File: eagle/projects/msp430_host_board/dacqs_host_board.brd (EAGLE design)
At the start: 127 x 102 mm, 165 parts, among them J1 MOL-SL-4-RA, J10 MOL-SL-3-V, J13 JST-PH-2TH-RA, J14 USB_MICROB_RECPT, J16 MOL-SL-2-RA, J17 CLM-112-02-L-D-IMU-MOUNT_IMU, J18 MOLSL-7-RA, J2 MOL-SL-4-RA, J3 MOL-SL-4-RA, J4 MOL-SL-4-RA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

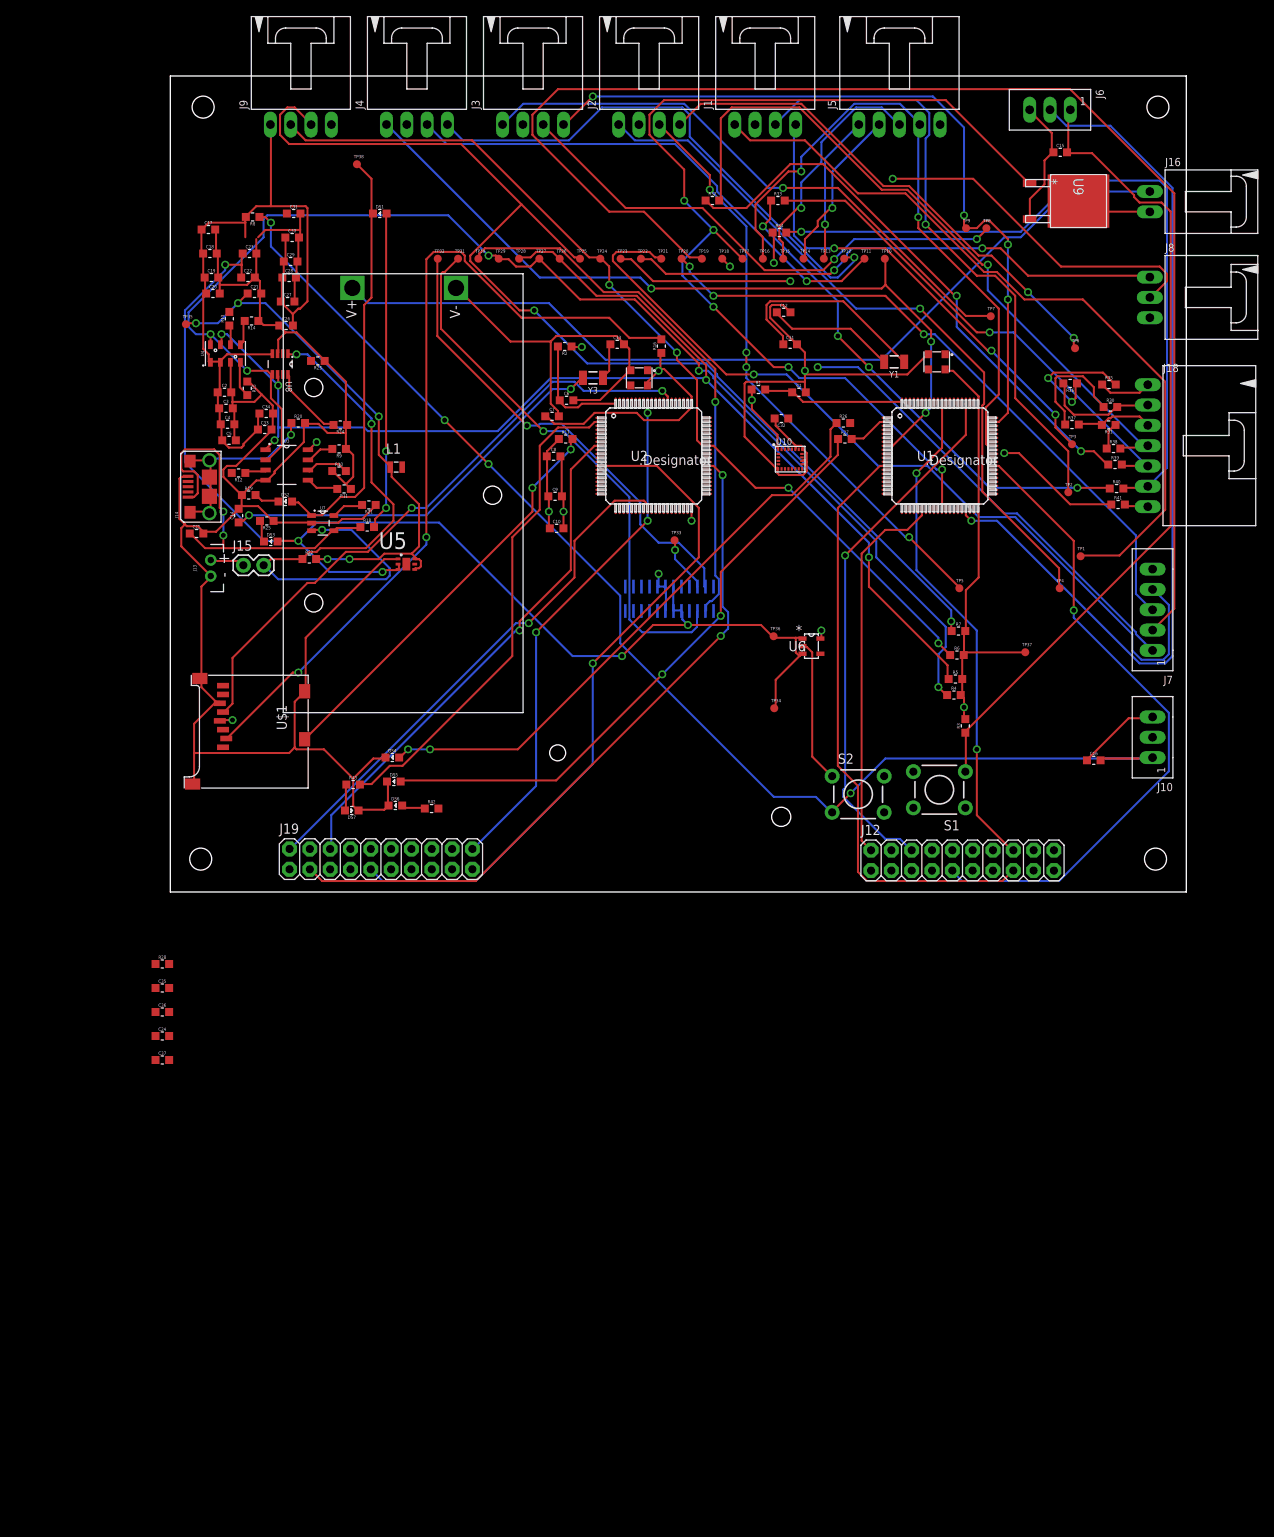
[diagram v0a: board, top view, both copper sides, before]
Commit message: Changed motor battery Vsense
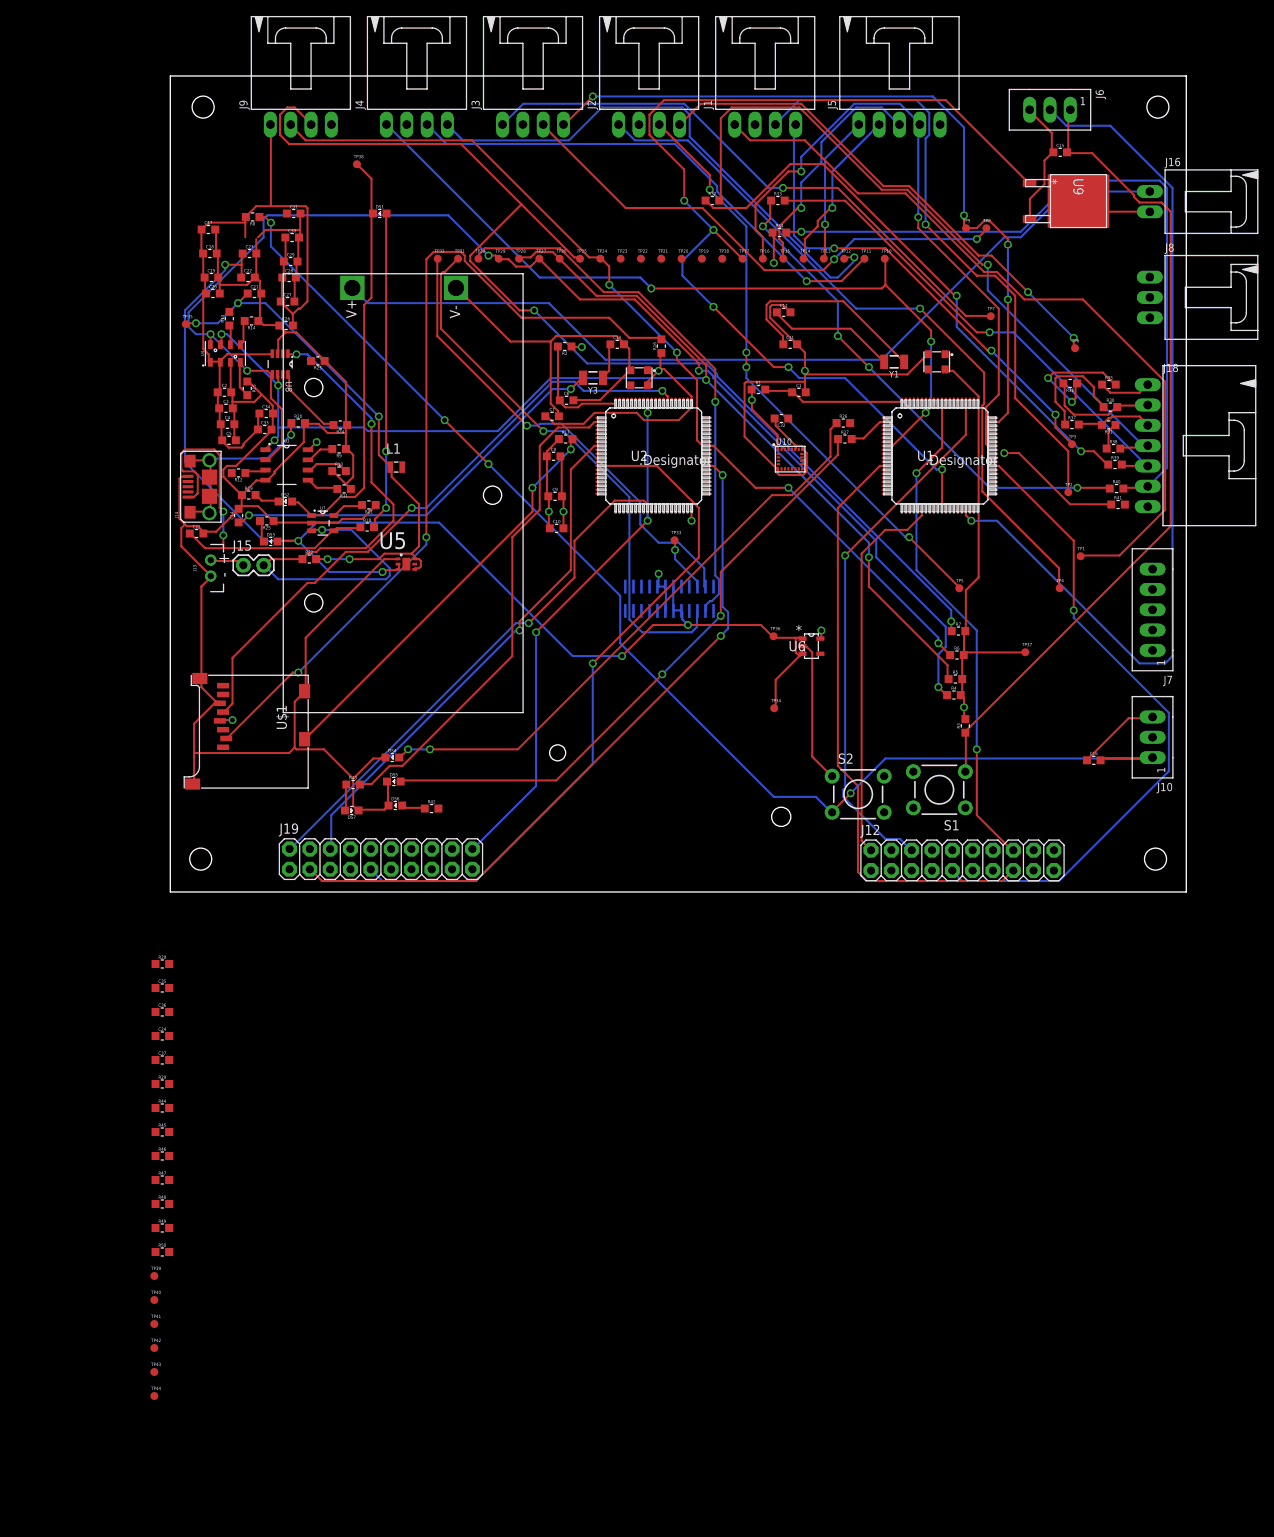
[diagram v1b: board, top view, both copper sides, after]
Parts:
- added R29, R44, R45, R46, R47, R48: 0, daqcs_host:R0603
- added R49, R50: 47k, daqcs_host:R0603
- added TP39, TP40, TP41, TP42, TP43, TP44: (no value), daqcs_host:TP10R
- R30: value 10k -> 60.4k
- R31: value 10k -> 69.8k
- R32, R33, R35: value 10k -> 49.9k
- R34: value 10k -> 12k
- R36: value 27k -> 7.15k
- R37: value 27k -> 10k
- R38, R39: value 27k -> 15k
- R40, R41: value 27k -> 30k
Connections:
- removed net VBAT_CELL_7: J18.7, R41.2
- new net ACT_CURRENT_IN_0: J8.2, R44.1
- new net ACT_SPEED_IN_0: J8.1, R29.1
- new net COMMS_MISO_0: J7.3, R47.1
- new net COMMS_MOSI_0: J7.4, R48.1
- new net COMMS_SCLK_0: J7.2, R46.1
- new net COMMS_SS_0: J7.1, R45.1
- new net RST_S1: R49.1, S1.3
- new net RST_S2: R50.1, S2.3
- net +3V3: now also J12.2
- net ACT_CURRENT_IN: now also R44.2; no longer J8.2
- net ACT_SPEED_IN: now also R29.2; no longer J8.1
- net COMMS_MISO: now also R47.2, TP20.TP
- net COMMS_MOSI: now also R48.2, TP21.TP
- net COMMS_SCLK: now also R46.2, TP19.TP
- net COMMS_SS: now also R45.2, TP18.TP
- net CURRENT_PWM_OUT: no longer J7.2, TP19.TP
- net DIR_MOTOR_OUT: no longer J7.4, TP21.TP
- net EN_MOTOR_OUT: no longer J7.3, TP20.TP
- net GND: now also J12.20, J18.7, TP39.TP, TP41.TP, TP42.TP, TP43.TP, TP44.TP
- net P2.3: no longer J12.4
- net P2.4: no longer J12.6
- net P4.1: now also J12.6; no longer J12.8
- net P6.2: now also J12.8; no longer J12.10
- net P6.3: now also J12.10; no longer J12.12
- net P6.4: now also J12.12; no longer J12.14
- net P6.5: now also J12.14; no longer J12.16
- net P6.6: now also J12.16; no longer J12.18
- net P6.7: now also J12.18; no longer J12.20
- net P7.3: now also J12.4; no longer J12.2
- net RST_SBWTDIO_HOST: now also R49.2; no longer S1.3
- net RST_SBWTDIO_MOTOR: now also R50.2; no longer S2.3
- net SPEED_PWM_OUT: no longer J7.1, TP18.TP
- net VBAT_CELL_2: no longer R36.2
- net VBAT_CELL_3: no longer R37.2
- net VBAT_CELL_4: no longer R38.2
- net VBAT_CELL_5: no longer R39.2
- net VBAT_CELL_6: no longer R40.2
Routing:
- net CURRENT_PWM_OUT: track 172.8 -> 0.00 mm
- net DIR_MOTOR_OUT: track 107.9 -> 0.00 mm, vias 1 -> 0
- net ACT_CURRENT_IN: track 83.6 -> 0.00 mm, vias 2 -> 0
- net EN_MOTOR_OUT: track 81.8 -> 0.00 mm, vias 3 -> 0
- net SPEED_PWM_OUT: track 75.2 -> 0.00 mm, vias 2 -> 0
- net ACT_SPEED_IN: track 67.5 -> 0.00 mm, vias 2 -> 0
- net VBAT_CELL_7: track 3.06 -> 0.00 mm

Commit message: Added optocoupler isolation for cutdown mechanism
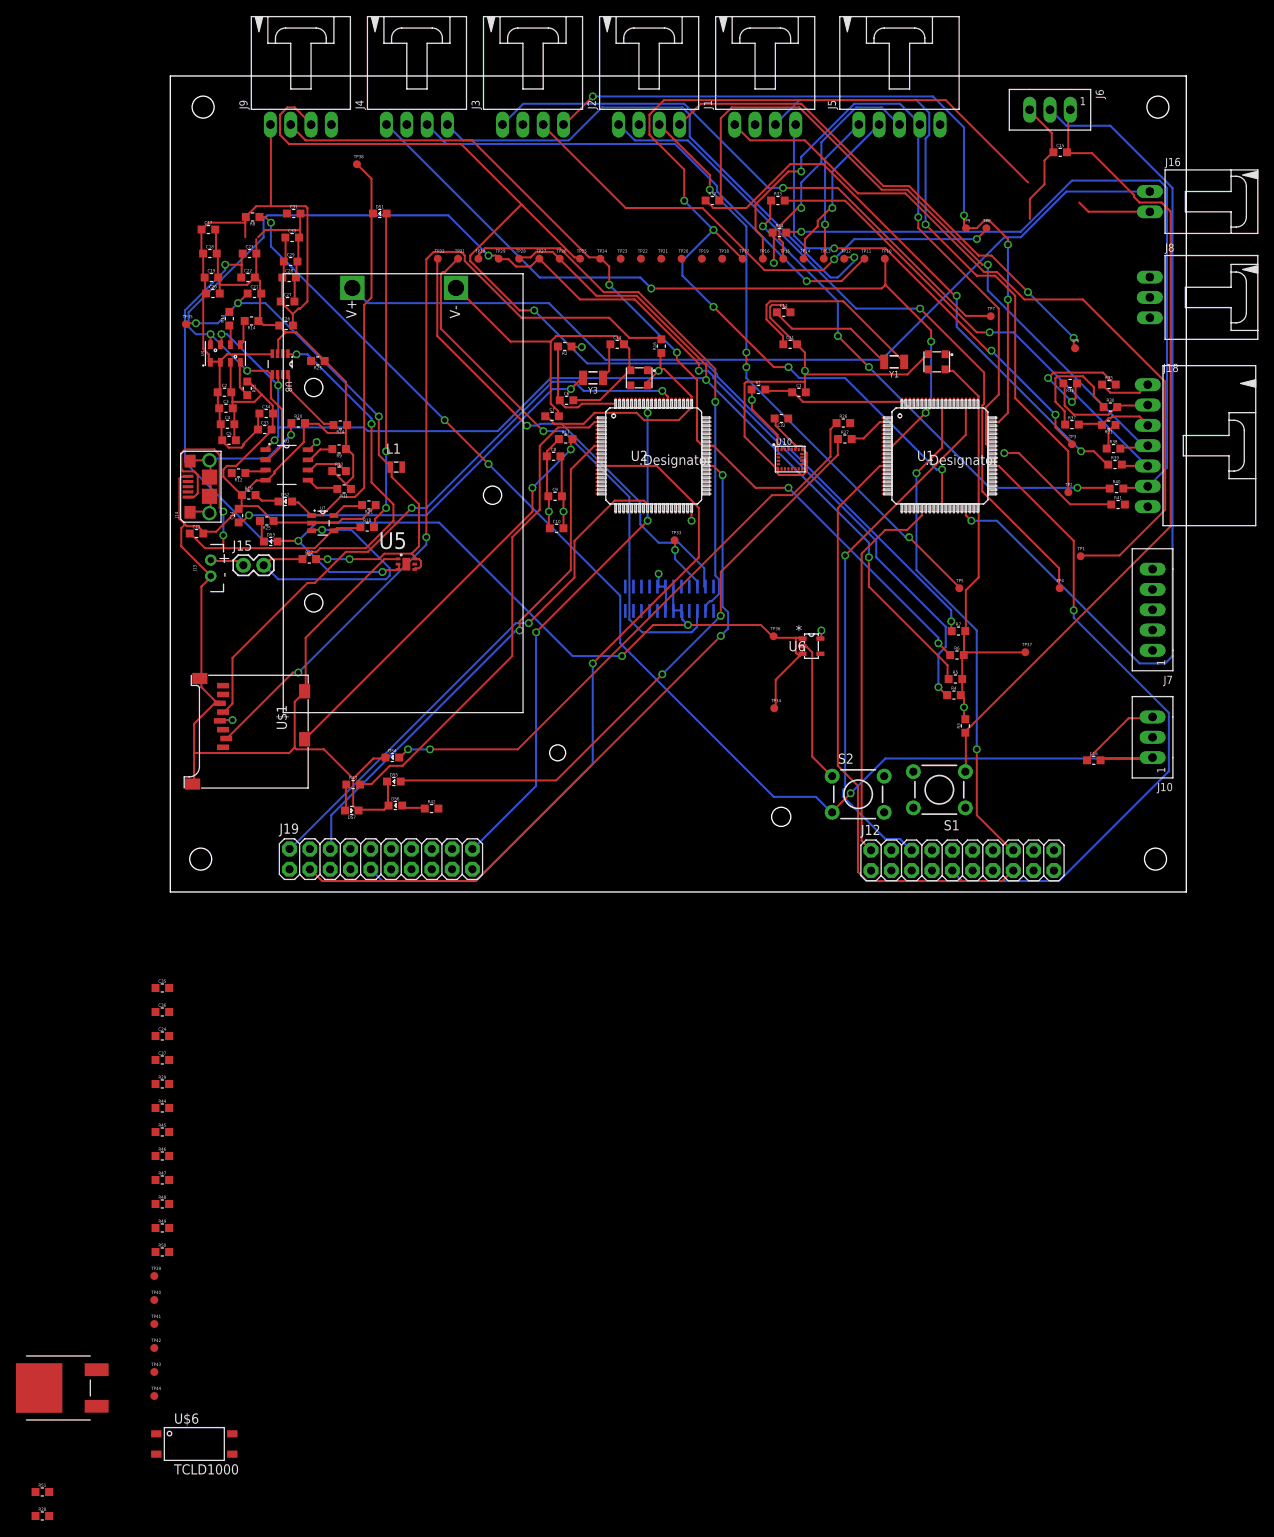
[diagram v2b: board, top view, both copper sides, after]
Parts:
- removed U9: STD12NF06LT4, daqcs_host:DPAK
- added R51: 47k, daqcs_host:R0603
- added U$6: TCLD1000, daqcs_host:TCLD1000
- added U$7: NTD2955T4G, daqcs_host:NTD2955T4G
- R28: value 10k -> 49.9k
- moved R28 70.6 mm to (-16.0, -78.0)
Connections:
- new net N$37: BAT1.V-, U$6.P$4, U$7.P$3
- new net N$59: R28.2, U$6.P$2
- net CUTDOWN_EN: now also R51.1, U$6.P$1, U$6.P$3, U$7.P$1; no longer R28.2, U9.1
- net GND: no longer BAT1.V-, U9.2
- net N$6: now also R51.2, U$7.P$2; no longer U9.3

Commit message: Pinned the IMU2 interrupt signals to the GPIO headers
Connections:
- removed net N$22: U10.9
- removed net N$23: U10.10
- removed net N$7: U10.11
- removed net N$8: U10.12
- removed net N$9: U10.13
- new net IMU2_DEN: J12.11, U10.13
- new net IMU2_DRDY: J12.13, U10.9
- new net IMU2_INT1: J12.7, U10.11
- new net IMU2_INT2: J12.9, U10.12
- new net IMU2_INT_M: J12.15, U10.10
- new net N$60: U1.27
- net P3.4: no longer J12.7
- net P3.5: no longer J12.9
- net P4.1: no longer J12.6
- net P5.6: no longer J12.11
- net P5.7: no longer J12.13
- net P7.0: now also J12.17; no longer J12.15
- net P7.1: now also J12.19; no longer J12.17
- net P7.2: now also J12.4; no longer J12.19
- net P7.3: now also J12.6; no longer J12.4
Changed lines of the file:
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@@
 <signal name="P7.0">
 <contactref element="U1" pad="13"/>
-<contactref element="J12" pad="15"/>
 <wire x1="88.6968" y1="53.2638" x2="89.3826" y2="53.2638" width="0.254" layer="1"/>
 <wire x1="83.439" y1="48.006" x2="88.6968" y2="53.2638" width="0.254" layer="1"/>
@@
 <wire x1="105.156" y1="2.5146" x2="104.013" y2="1.3716" width="0.254" layer="1"/>
 <wire x1="89.3826" y1="53.2638" x2="89.475" y2="53.27" width="0.254" layer="1"/>
-<wire x1="105.156" y1="2.5146" x2="105.37" y2="2.68" width="0.254" layer="1"/>
+<contactref element="J12" pad="17"/>
+<wire x1="105.156" y1="2.5146" x2="107.91" y2="2.68" width="0" layer="19" extent="1-1"/>
 </signal>
 <signal name="P7.1">
 <contactref element="U1" pad="14"/>
-<contactref element="J12" pad="17"/>
-<wire x1="107.91" y1="2.68" x2="89.475" y2="52.77" width="0" layer="19" extent="1-1"/>
+<contactref element="J12" pad="19"/>
+<wire x1="110.45" y1="2.68" x2="89.475" y2="52.77" width="0" layer="19" extent="1-1"/>
 </signal>
 <signal name="P7.2">
 <contactref element="U1" pad="25"/>
-<contactref element="J12" pad="19"/>
-<wire x1="110.45" y1="2.68" x2="93.45" y2="47.795" width="0" layer="19" extent="1-1"/>
+<contactref element="J12" pad="4"/>
+<wire x1="90.13" y1="5.22" x2="93.45" y2="47.795" width="0" layer="19" extent="1-1"/>
 </signal>
 <signal name="P7.3">
@@
 <wire x1="87.5538" y1="5.2578" x2="86.4108" y2="6.4008" width="0.254" layer="1"/>
 <wire x1="93.9546" y1="47.7774" x2="93.95" y2="47.795" width="0.254" layer="1"/>
-<contactref element="J12" pad="4"/>
-<wire x1="87.5538" y1="5.2578" x2="90.13" y2="5.22" width="0" layer="19" extent="1-1"/>
+<contactref element="J12" pad="6"/>
+<wire x1="87.5538" y1="5.2578" x2="92.67" y2="5.22" width="0" layer="19" extent="1-1"/>
 </signal>
 <signal name="P3.4">
 <contactref element="U1" pad="47"/>
-<contactref element="J12" pad="7"/>
-<wire x1="95.21" y1="2.68" x2="102.925" y2="52.77" width="0" layer="19" extent="1-1"/>
 </signal>
 <signal name="P3.5">
 <contactref element="U1" pad="48"/>
-<contactref element="J12" pad="9"/>
 <wire x1="103.5558" y1="53.2638" x2="103.0986" y2="53.2638" width="0.254" layer="1"/>
 <wire x1="112.9284" y1="43.8912" x2="103.5558" y2="53.2638" width="0.254" layer="1"/>
@@
 <wire x1="97.8408" y1="2.5146" x2="98.9838" y2="1.3716" width="0.254" layer="16"/>
 <wire x1="103.0986" y1="53.2638" x2="102.925" y2="53.27" width="0.254" layer="1"/>
-<wire x1="97.8408" y1="2.5146" x2="97.75" y2="2.68" width="0.254" layer="16"/>
 <via x="112.9284" y="35.2044" extent="1-16" drill="0.6096"/>
 </signal>
 <signal name="P5.6">
 <contactref element="U1" pad="67"/>
-<contactref element="J12" pad="11"/>
-<wire x1="100.29" y1="2.68" x2="97.95" y2="61.245" width="0" layer="19" extent="1-1"/>
 </signal>
 <signal name="P5.7">
 <contactref element="U1" pad="68"/>
-<contactref element="J12" pad="13"/>
-<wire x1="102.83" y1="2.68" x2="97.45" y2="61.245" width="0" layer="19" extent="1-1"/>
 </signal>
 <signal name="P2.3">
@@
 <signal name="P4.1">
 <contactref element="U1" pad="32"/>
-<contactref element="J12" pad="6"/>
-<wire x1="92.67" y1="5.22" x2="96.95" y2="47.795" width="0" layer="19" extent="1-1"/>
 </signal>
 <signal name="N$10">
@@
 <wire x1="14.57" y1="84.81" x2="76.405" y2="55.335" width="0" layer="19" extent="1-1"/>
 </signal>
-<signal name="N$7">
+<signal name="IMU2_INT1">
 <contactref element="U10" pad="11"/>
-</signal>
-<signal name="N$8">
+<contactref element="J12" pad="7"/>
+<wire x1="95.21" y1="2.68" x2="78.125" y2="52.885" width="0" layer="19" extent="1-1"/>
+</signal>
+<signal name="IMU2_INT2">
 <contactref element="U10" pad="12"/>
-</signal>
-<signal name="N$9">
+<contactref element="J12" pad="9"/>
+<wire x1="97.75" y1="2.68" x2="78.555" y2="52.885" width="0" layer="19" extent="1-1"/>
+</signal>
+<signal name="IMU2_DEN">
 <contactref element="U10" pad="13"/>
-</signal>
-<signal name="N$22">
+<contactref element="J12" pad="11"/>
+<wire x1="100.29" y1="2.68" x2="78.985" y2="52.885" width="0" layer="19" extent="1-1"/>
+</signal>
+<signal name="IMU2_DRDY">
 <contactref element="U10" pad="9"/>
-</signal>
-<signal name="N$23">
+<contactref element="J12" pad="13"/>
+<wire x1="102.83" y1="2.68" x2="77.265" y2="52.885" width="0" layer="19" extent="1-1"/>
+</signal>
+<signal name="IMU2_INT_M">
 <contactref element="U10" pad="10"/>
+<contactref element="J12" pad="15"/>
+<wire x1="105.37" y1="2.68" x2="77.695" y2="52.885" width="0" layer="19" extent="1-1"/>
 </signal>
 <signal name="N$47">
@@
 <wire x1="-1.75" y1="-70.27" x2="-15.15" y2="-78" width="0" layer="19" extent="1-1"/>
 </signal>
+<signal name="N$60">
+<contactref element="U1" pad="27"/>
+</signal>
 </signals>

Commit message: Small change
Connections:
- net N$37 renamed 9V_GND
- net N$59 renamed OPTO_OUT
- net N$6 renamed CUTDOWN_DRAIN
- new net CUTDOWN_GATE: R51.1, U$6.P$3, U$7.P$1
- net CUTDOWN_EN: no longer R51.1, U$6.P$3, U$7.P$1
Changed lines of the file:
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@@
 <via x="77.2668" y="65.6082" extent="1-16" drill="0.6096"/>
 <via x="67.8942" y="73.152" extent="1-16" drill="0.6096"/>
-<contactref element="U$7" pad="P$1"/>
-<contactref element="R51" pad="1"/>
-<contactref element="U$6" pad="P$3"/>
 <contactref element="U$6" pad="P$1"/>
 <contactref element="TP17" pad="TP"/>
 <wire x1="71.3232" y1="79.3242" x2="71.53" y2="79.16" width="0" layer="19" extent="1-1"/>
-<wire x1="7.75" y1="-70.27" x2="96.45" y2="47.795" width="0" layer="19" extent="1-1"/>
-<wire x1="-1.75" y1="-67.73" x2="7.75" y2="-70.27" width="0" layer="19" extent="1-1"/>
-<wire x1="-9.21" y1="-64.285" x2="-1.75" y2="-67.73" width="0" layer="19" extent="1-1"/>
-<wire x1="-16.85" y1="-75" x2="-9.21" y2="-64.285" width="0" layer="19" extent="1-1"/>
+<wire x1="-1.75" y1="-67.73" x2="96.45" y2="47.795" width="0" layer="19" extent="1-1"/>
 </signal>
 <signal name="VBAT_MOD_CELL_1">
@@
 <wire x1="22.86" y1="75.438" x2="22.754" y2="75.506" width="0.254" layer="16"/>
 </signal>
-<signal name="N$6">
+<signal name="CUTDOWN_DRAIN">
 <contactref element="J16" pad="2"/>
 <wire x1="114.7572" y1="85.0392" x2="122.301" y2="85.0392" width="0.254" layer="1"/>
@@
 <wire x1="-1.85" y1="-45" x2="82.7288" y2="9.9594" width="0" layer="19" extent="1-1"/>
 </signal>
-<signal name="N$37">
+<signal name="9V_GND">
 <contactref element="U$7" pad="P$3"/>
 <contactref element="BAT1" pad="V-"/>
@@
 <wire x1="-16.39" y1="-62" x2="7.75" y2="-67.73" width="0" layer="19" extent="1-1"/>
 </signal>
-<signal name="N$59">
+<signal name="OPTO_OUT">
 <contactref element="U$6" pad="P$2"/>
 <contactref element="R28" pad="2"/>
@@
 <contactref element="U1" pad="27"/>
 </signal>
+<signal name="CUTDOWN_GATE">
+<contactref element="U$7" pad="P$1"/>
+<contactref element="R51" pad="1"/>
+<contactref element="U$6" pad="P$3"/>
+<wire x1="-9.21" y1="-64.285" x2="-16.85" y2="-75" width="0" layer="19" extent="1-1"/>
+<wire x1="7.75" y1="-70.27" x2="-9.21" y2="-64.285" width="0" layer="19" extent="1-1"/>
+</signal>
 </signals>
